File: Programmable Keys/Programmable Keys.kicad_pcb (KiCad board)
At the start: 2 copper layers, 69.1 x 57.1 mm, 22 parts, among them J1 Conn_01x05_Female, J2 Conn_01x05_Male

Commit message: Started wiring
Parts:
- moved D7 0.79 mm to (244.5, 77.8)
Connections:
- J1 pad 2: unconnected-(J1-Pad2) -> VCC
- J2 pad 2: unconnected-(J2-Pad2) -> VCC
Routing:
- net ROW2: track 0.00 -> 44.5 mm
- net ROW1: track 0.00 -> 44.5 mm, vias 0 -> 4
- net ROW0: track 0.00 -> 44.5 mm, vias 0 -> 4
- net COL2: track 0.00 -> 38.1 mm
- net COL1: track 0.00 -> 38.1 mm
- net COL0: track 0.00 -> 38.1 mm
- net Net-(D7-Pad2): track 0.00 -> 7.51 mm
- net Net-(D1-Pad2): track 0.00 -> 7.51 mm
- net Net-(D4-Pad2): track 0.00 -> 7.51 mm
- net Net-(D8-Pad2): track 0.00 -> 7.51 mm
- net Net-(D2-Pad2): track 0.00 -> 7.51 mm
- net Net-(D9-Pad2): track 0.00 -> 7.51 mm
- net Net-(D3-Pad2): track 0.00 -> 7.51 mm
- net Net-(D5-Pad2): track 0.00 -> 7.51 mm
- net Net-(D6-Pad2): track 0.00 -> 7.51 mm

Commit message: Started wiring
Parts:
- removed R1, R2: 100, Resistor_SMD:R_0805_2012Metric
- J1: value Conn_01x05_Female -> Conn_01x19_Female; footprint Connector_JST:JST_PH_B5B-PH-K_1x05_P2.00mm_Vertical -> Connector_JST:JST_SH_SM20B-SRSS-TB_1x20-1MP_P1.00mm_Horizontal
- J2: value Conn_01x05_Male -> Conn_01x19_Male; footprint Connector_JST:JST_PH_B5B-PH-K_1x05_P2.00mm_Vertical -> Connector_JST:JST_SH_SM20B-SRSS-TB_1x20-1MP_P1.00mm_Horizontal
- moved J1 4.53 mm to (186.5, 96.8), turned to 90 degrees
- moved J2 4.20 mm to (249.2, 96.8), turned to -90 degrees
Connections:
- D1 pad 1: ROW0 -> ROW5
- D2 pad 1: ROW1 -> ROW6
- D3 pad 1: ROW2 -> ROW7
- D4 pad 1: ROW0 -> ROW5
- D5 pad 1: ROW1 -> ROW6
- D6 pad 1: ROW2 -> ROW7
- D7 pad 1: ROW0 -> ROW5
- D8 pad 1: ROW1 -> ROW6
- D9 pad 1: ROW2 -> ROW7
- J1 pad 1: VCC -> +5V
- J1 pad 3: Net-(J1-Pad3) -> COL0
- J1 pad 4: unconnected-(J1-Pad4) -> COL1
- J1 pad 5: GND -> COL2
- J2 pad 1: VCC -> +5V
- J2 pad 3: Net-(J2-Pad3) -> COL0
- J2 pad 4: unconnected-(J2-Pad4) -> COL1
- J2 pad 5: GND -> COL2
- MX1 pad 1: COL0 -> COL8
- MX2 pad 1: COL1 -> COL9
- MX3 pad 1: COL2 -> COL10
- MX4 pad 1: COL0 -> COL8
- MX5 pad 1: COL1 -> COL9
- MX6 pad 1: COL2 -> COL10
- MX7 pad 1: COL0 -> COL8
- MX8 pad 1: COL1 -> COL9
- MX9 pad 1: COL2 -> COL10
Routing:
- net GND: track 0.00 -> 129.9 mm, vias 0 -> 2
- net COL6: track 0.00 -> 129.5 mm, vias 0 -> 7
- net COL5: track 0.00 -> 127.2 mm, vias 0 -> 6
- net COL8: track 0.00 -> 121.2 mm, vias 0 -> 7
- net ROW7: track 0.00 -> 116.9 mm, vias 0 -> 4
- net COL10: track 0.00 -> 109.8 mm, vias 0 -> 12
- net COL9: track 0.00 -> 109.2 mm, vias 0 -> 6
- net ROW5: track 0.00 -> 102.7 mm, vias 0 -> 6
- net ROW9: track 0.00 -> 83.1 mm, vias 0 -> 8
- net ROW8: track 0.00 -> 82.9 mm, vias 0 -> 12
- net ROW6: track 0.00 -> 82.7 mm, vias 0 -> 6
- net COL7: track 0.00 -> 76.6 mm, vias 0 -> 9
- net COL4: track 0.00 -> 76.0 mm, vias 0 -> 9
- net ROW2: track 44.5 -> 0.00 mm
- net ROW1: track 44.5 -> 0.00 mm, vias 4 -> 0
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
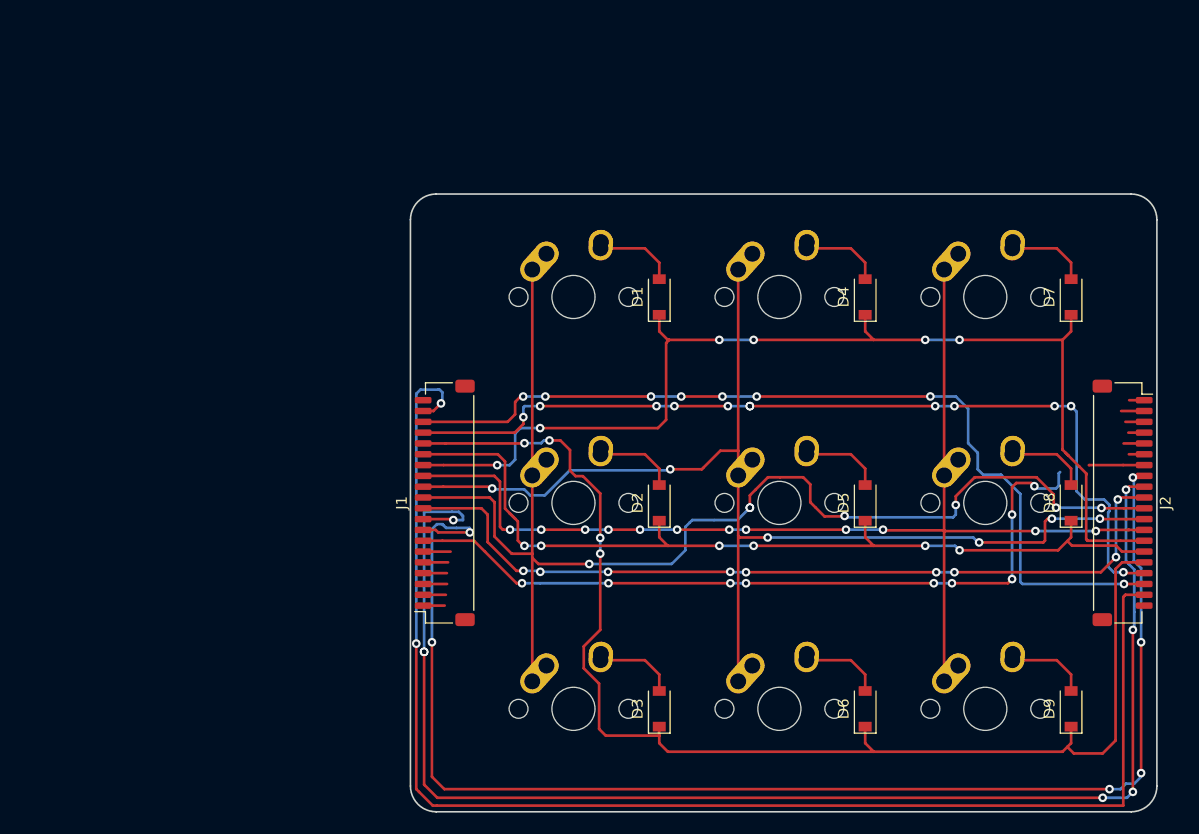
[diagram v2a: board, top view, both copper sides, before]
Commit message: Restarted wiring
Wiring was gonna be a pain so I decided to restart and do it better
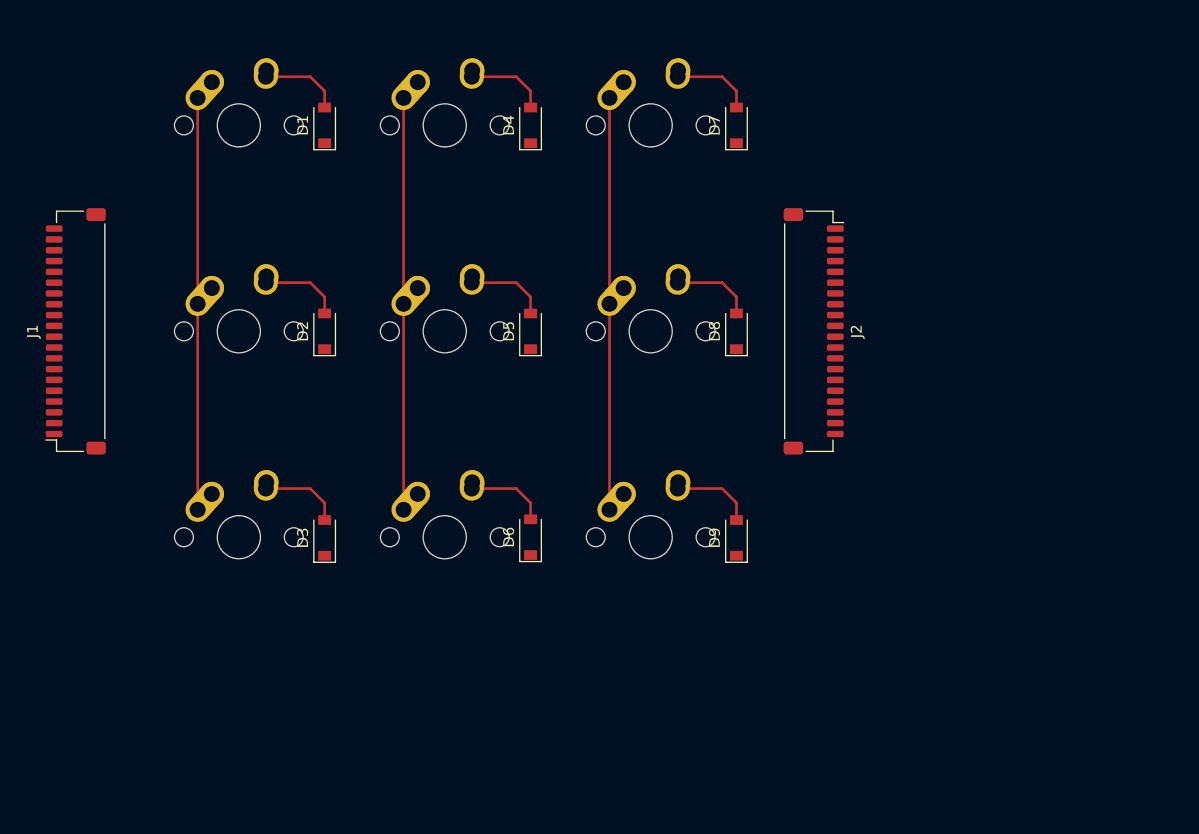
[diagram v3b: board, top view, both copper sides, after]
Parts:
- moved J1 37.6 mm to (152.4, 81.0)
- moved D1 34.8 mm to (175.4, 61.9)
- moved D2 34.8 mm to (175.4, 81.0)
- moved D4 34.8 mm to (194.5, 61.9)
- moved D5 34.8 mm to (194.5, 81.0)
- moved D6 34.8 mm to (194.5, 100.0)
- moved MX1 34.8 mm to (167.5, 61.9)
- moved MX2 34.8 mm to (186.5, 61.9)
- moved MX4 34.8 mm to (167.5, 81.0)
- moved MX5 34.8 mm to (186.5, 81.0)
- moved MX7 34.8 mm to (167.5, 100.0)
- moved MX8 34.8 mm to (186.5, 100.0)
- moved D7 34.8 mm to (213.5, 61.9)
- moved D8 34.8 mm to (213.5, 81.0)
- moved MX3 34.8 mm to (205.6, 61.9)
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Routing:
- net GND: track 129.9 -> 0.00 mm, vias 2 -> 0
- net COL6: track 129.5 -> 0.00 mm, vias 7 -> 0
- net COL5: track 127.2 -> 0.00 mm, vias 6 -> 0
- net ROW7: track 116.9 -> 0.00 mm, vias 4 -> 0
- net ROW5: track 102.7 -> 0.00 mm, vias 6 -> 0
- net COL8: track 121.2 -> 38.1 mm, vias 7 -> 0
- net ROW9: track 83.1 -> 0.00 mm, vias 8 -> 0
- net ROW8: track 82.9 -> 0.00 mm, vias 12 -> 0
- net ROW6: track 82.7 -> 0.00 mm, vias 6 -> 0
- net COL7: track 76.6 -> 0.00 mm, vias 9 -> 0
- net COL4: track 76.0 -> 0.00 mm, vias 9 -> 0
- net COL10: track 109.8 -> 38.1 mm, vias 12 -> 0
- net COL9: track 109.2 -> 38.1 mm, vias 6 -> 0
- net VCC: track 4.24 -> 0.00 mm
- net COL2: track 4.22 -> 0.00 mm
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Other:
- board outline removed

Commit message: Finished wiring
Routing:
- net ROW7: track 0.00 -> 127.8 mm, vias 0 -> 2
- net ROW5: track 0.00 -> 118.1 mm, vias 0 -> 8
- net +5V: track 0.00 -> 98.1 mm, vias 0 -> 8
- net VCC: track 0.00 -> 96.8 mm, vias 0 -> 8
- net COL9: track 38.1 -> 134.3 mm, vias 0 -> 8
- net COL1: track 0.00 -> 93.6 mm, vias 0 -> 8
- net ROW6: track 0.00 -> 89.6 mm, vias 0 -> 8
- net COL0: track 0.00 -> 89.5 mm, vias 0 -> 8
- net GND: track 0.00 -> 89.3 mm, vias 0 -> 6
- net COL8: track 38.1 -> 126.0 mm, vias 0 -> 10
- net ROW8: track 0.00 -> 86.7 mm, vias 0 -> 6
- net COL2: track 0.00 -> 85.1 mm, vias 0 -> 8
- net ROW9: track 0.00 -> 84.5 mm, vias 0 -> 6
- net COL3: track 0.00 -> 84.5 mm, vias 0 -> 8
- net COL10: track 38.1 -> 121.8 mm, vias 0 -> 8
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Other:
- board outline added: 76.2 x 57.1 mm

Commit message: Finished pcb
for now
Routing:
- added copper zone on B.Cu, net GND
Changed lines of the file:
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@@
   (segment (start 202.692 93.472) (end 200.914 93.472) (width 0.25) (layer "B.Cu") (net 28))
   (segment (start 222.377 93.472) (end 219.329 93.472) (width 0.25) (layer "B.Cu") (net 28))
+  (zone (net 16) (net_name "GND") (layer "B.Cu") (hatch edge 0.508)
+    (connect_pads (clearance 0.508))
+    (min_thickness 0.254) (filled_areas_thickness no)
+    (fill yes (thermal_gap 0.508) (thermal_bridge_width 0.508))
+    (polygon
+      (pts
+        (xy 157.95625 109.5375)
+        (xy 148.43125 109.5375)
+        (xy 148.43125 52.3875)
+        (xy 157.95625 52.3875)
+      )
+    )
+  )
+  (zone (net 16) (net_name "GND") (layer "B.Cu") (hatch edge 0.508)
+    (connect_pads (clearance 0.508))
+    (min_thickness 0.254) (filled_areas_thickness no)
+    (fill yes (thermal_gap 0.508) (thermal_bridge_width 0.508))
+    (polygon
+      (pts
+        (xy 224.63125 109.5375)
+        (xy 215.10625 109.5375)
+        (xy 215.10625 52.3875)
+        (xy 224.63125 52.3875)
+      )
+    )
+  )
 )
